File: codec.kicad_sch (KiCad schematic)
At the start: 16 parts, among them U1 PCM2906CDBR, Y1 12MHz

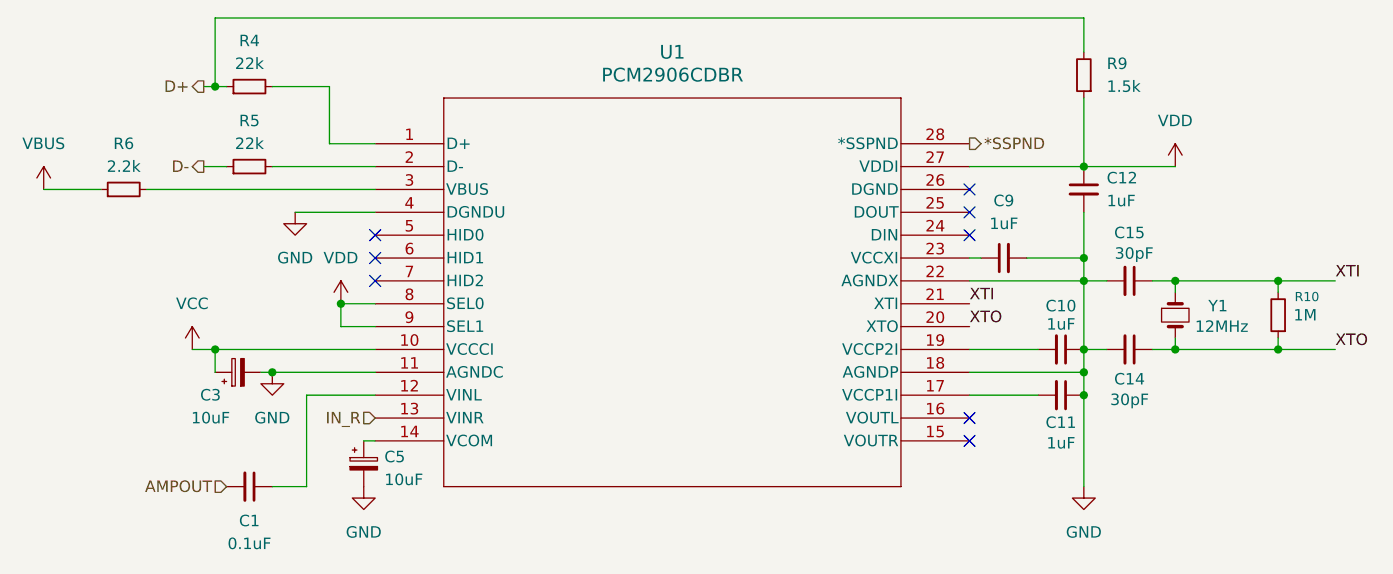
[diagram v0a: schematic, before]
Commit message: Add missing PCM2906 components; Partially Implement PCB
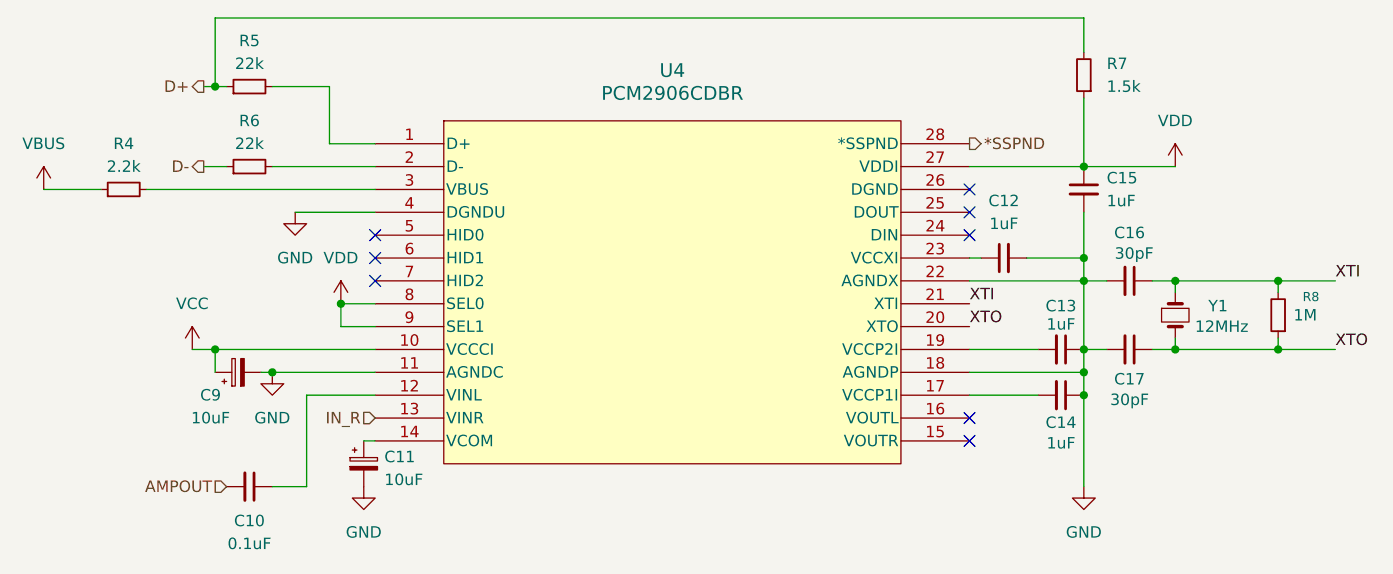
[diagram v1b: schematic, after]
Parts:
- C10: renamed from C1; footprint (none) -> Capacitor_SMD:C_0603_1608Metric_Pad1.08x0.95mm_HandSolder
- C11: renamed from C5; footprint (none) -> Capacitor_Tantalum_SMD:CP_EIA-3216-10_Kemet-I_HandSolder
- C12: renamed from C9; footprint (none) -> Capacitor_SMD:C_0603_1608Metric_Pad1.08x0.95mm_HandSolder
- C13: renamed from C10; footprint (none) -> Capacitor_SMD:C_0603_1608Metric_Pad1.08x0.95mm_HandSolder
- C14: renamed from C11; footprint (none) -> Capacitor_SMD:C_0603_1608Metric_Pad1.08x0.95mm_HandSolder
- C15: renamed from C12; footprint (none) -> Capacitor_SMD:C_0603_1608Metric_Pad1.08x0.95mm_HandSolder
- C16: renamed from C15; footprint (none) -> Capacitor_SMD:C_0603_1608Metric_Pad1.08x0.95mm_HandSolder
- C17: renamed from C14; footprint (none) -> Capacitor_SMD:C_0603_1608Metric_Pad1.08x0.95mm_HandSolder
- C9: renamed from C3; footprint (none) -> Capacitor_Tantalum_SMD:CP_EIA-3216-10_Kemet-I_HandSolder
- R4: renamed from R6; footprint (none) -> Resistor_SMD:R_0603_1608Metric_Pad0.98x0.95mm_HandSolder
- R5: renamed from R4; footprint (none) -> Resistor_SMD:R_0603_1608Metric_Pad0.98x0.95mm_HandSolder
- R6: renamed from R5; footprint (none) -> Resistor_SMD:R_0603_1608Metric_Pad0.98x0.95mm_HandSolder
- R7: renamed from R9; footprint (none) -> Resistor_SMD:R_0603_1608Metric_Pad0.98x0.95mm_HandSolder
- R8: renamed from R10; footprint (none) -> Resistor_SMD:R_0603_1608Metric_Pad0.98x0.95mm_HandSolder
- Y1: footprint (none) -> Crystal:Crystal_HC49-4H_Vertical
- renumbered U1 to U4
